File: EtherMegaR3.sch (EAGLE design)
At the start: 49 parts, among them IC2 APX811-44UG-7, IC4 MCP24AA025E48, IC6 W5100SQFP80, IC9 ATMEGA2560-16AU, Q3 2N7002, U1 HY931147C-RJ45, X2 25MHz, X3 16MHz

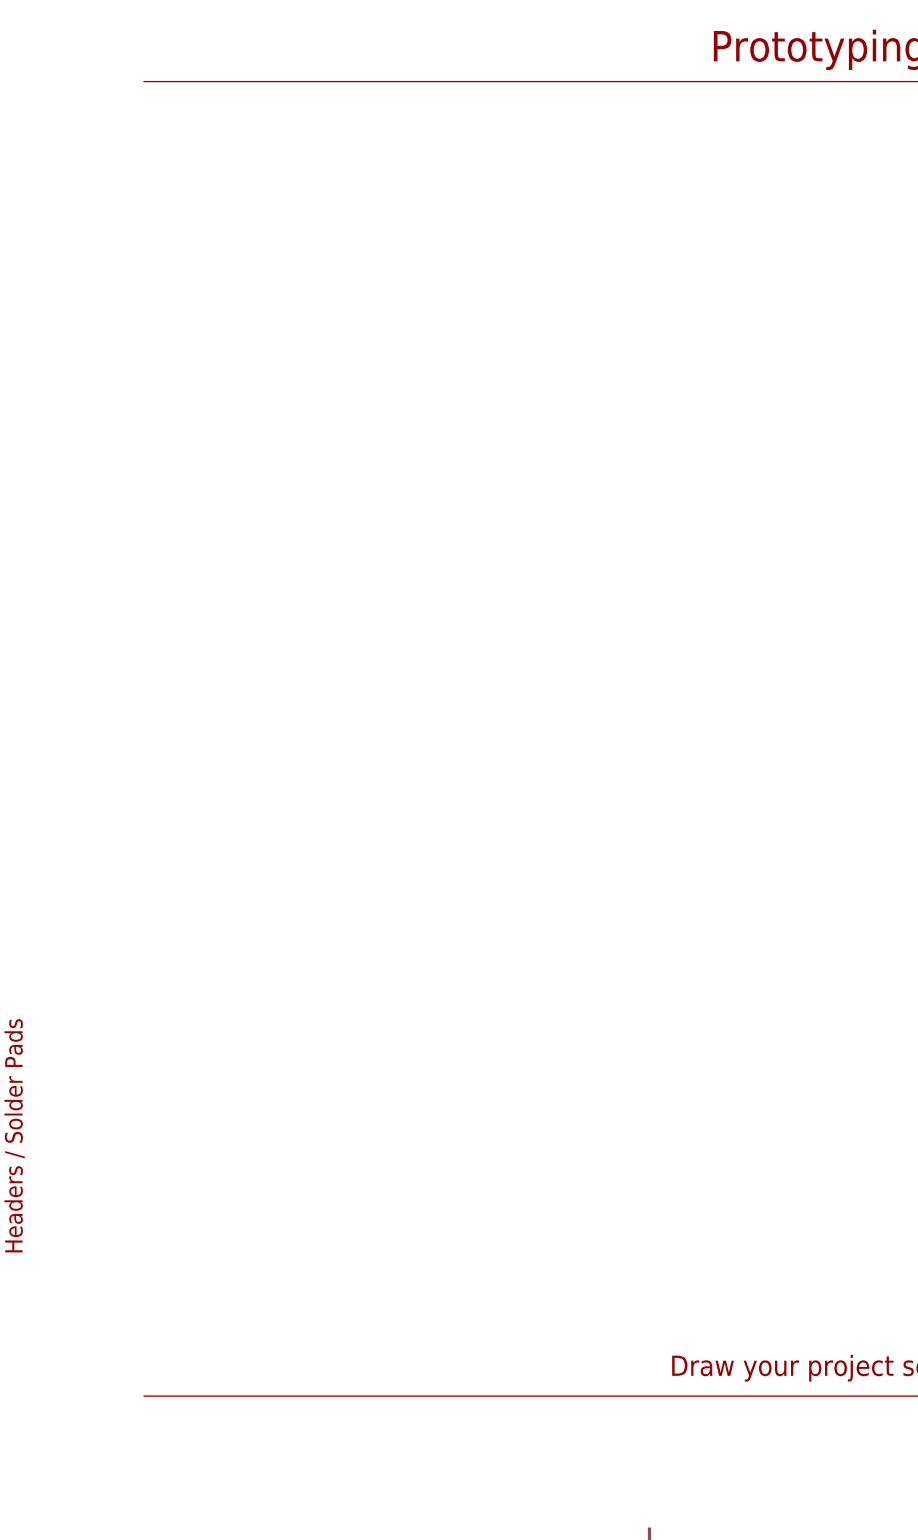
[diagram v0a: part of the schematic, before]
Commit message: remove eagle.epf
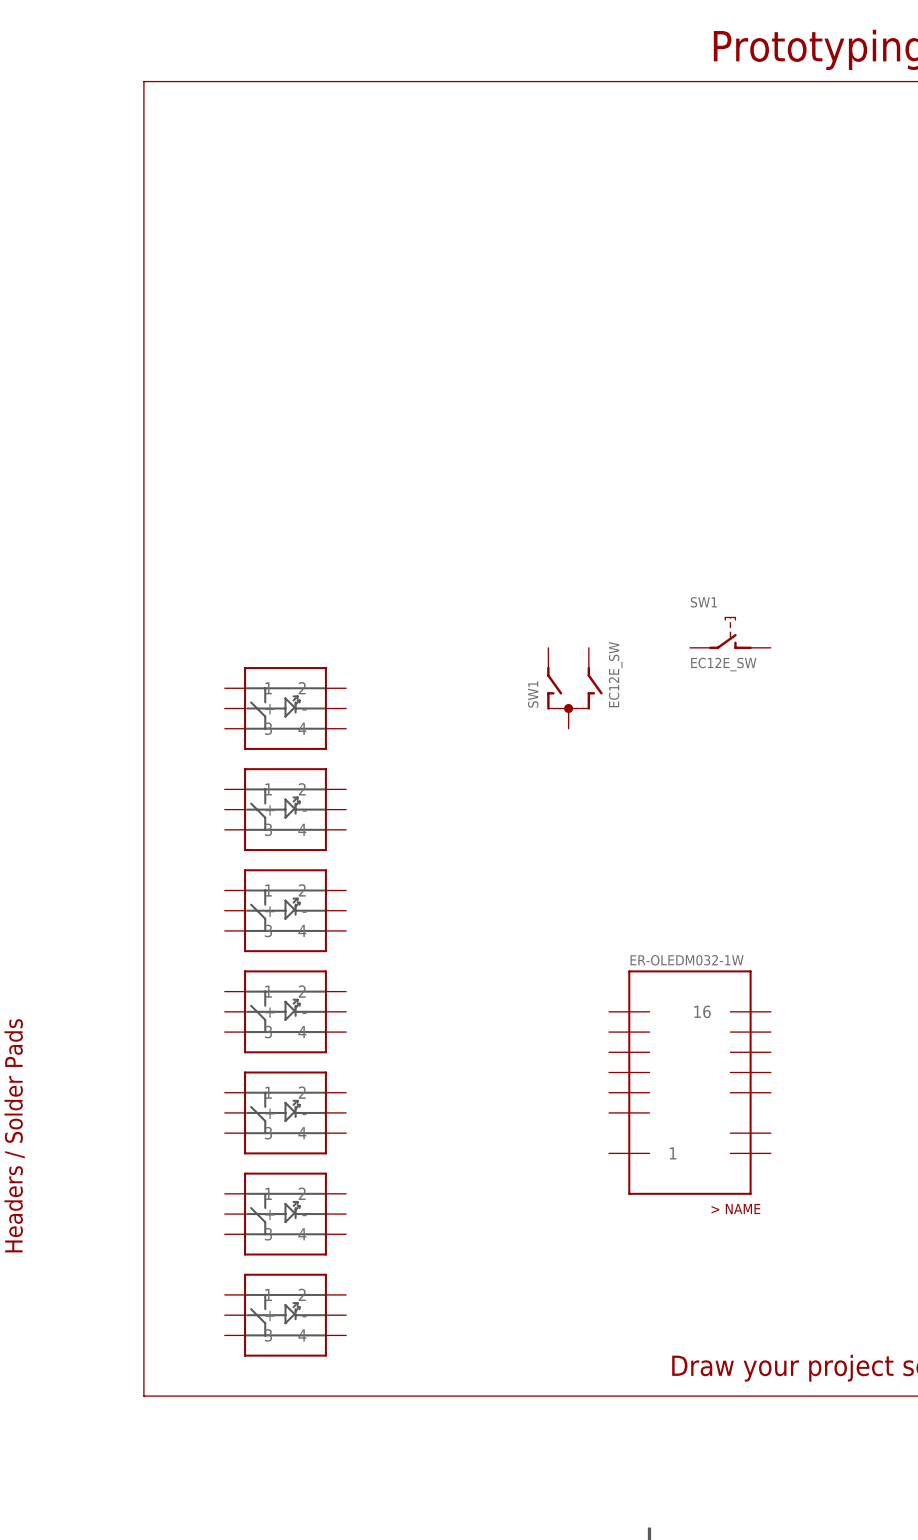
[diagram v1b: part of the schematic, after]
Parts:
- added BTN_FAVE1, BTN_FAVE2, BTN_FAVE3, BTN_FAVE4, BTN_FAVE5, BTN_MODE, BTN_OFF: PB614, RSJ-PB614:PB614
- added SW1: EC12E_SW, switch-alps:EC12E_SW
- added U$1: ER-OLED-M032-1W, Mat-Library:ER-OLED-M032-1W
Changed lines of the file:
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@@
 <layer number="54" name="bGND_GNDA" color="1" fill="9" visible="no" active="no"/>
 <layer number="56" name="wert" color="7" fill="1" visible="no" active="no"/>
+<layer number="90" name="Modules" color="5" fill="1" visible="yes" active="yes"/>
 <layer number="91" name="Nets" color="2" fill="1" visible="yes" active="yes"/>
 <layer number="92" name="Busses" color="1" fill="1" visible="yes" active="yes"/>
@@
 <part name="SJ5" library="freetronics-jon" deviceset="SJC" device="N" value=""/>
 <part name="SJ6" library="freetronics-jon" deviceset="SJC" device="N" value=""/>
+<part name="BTN_FAVE1" library="RSJ-PB614" deviceset="PB614" device=""/>
+<part name="BTN_FAVE2" library="RSJ-PB614" deviceset="PB614" device=""/>
+<part name="BTN_FAVE3" library="RSJ-PB614" deviceset="PB614" device=""/>
+<part name="BTN_FAVE4" library="RSJ-PB614" deviceset="PB614" device=""/>
+<part name="BTN_FAVE5" library="RSJ-PB614" deviceset="PB614" device=""/>
+<part name="BTN_MODE" library="RSJ-PB614" deviceset="PB614" device=""/>
+<part name="BTN_OFF" library="RSJ-PB614" deviceset="PB614" device=""/>
+<part name="U$1" library="Mat-Library" deviceset="ER-OLED-M032-1W" device=""/>
+<part name="SW1" library="switch-alps" deviceset="EC12E_SW" device=""/>
 </parts>
 <sheets>
@@
 <wire x1="416.56" y1="59.69" x2="416.56" y2="21.59" width="0.4064" layer="97" style="longdash"/>
 <wire x1="462.28" y1="69.85" x2="417.83" y2="69.85" width="0.4064" layer="97" style="longdash"/>
+<wire x1="25.4" y1="198.12" x2="25.4" y2="363.22" width="0.1524" layer="94"/>
 </plain>
 <instances>
@@
 <instance part="SJ5" gate="G$1" x="449.58" y="297.18"/>
 <instance part="SJ6" gate="G$1" x="449.58" y="289.56"/>
+<instance part="BTN_FAVE1" gate="G$1" x="40.64" y="208.28"/>
+<instance part="BTN_FAVE2" gate="G$1" x="40.64" y="220.98"/>
+<instance part="BTN_FAVE3" gate="G$1" x="40.64" y="233.68"/>
+<instance part="BTN_FAVE4" gate="G$1" x="40.64" y="246.38"/>
+<instance part="BTN_FAVE5" gate="G$1" x="40.64" y="259.08"/>
+<instance part="BTN_MODE" gate="G$1" x="40.64" y="271.78"/>
+<instance part="BTN_OFF" gate="G$1" x="40.64" y="284.48"/>
+<instance part="U$1" gate="G$1" x="93.98" y="236.22"/>
+<instance part="SW1" gate="G$1" x="78.74" y="284.48"/>
+<instance part="SW1" gate="G$2" x="99.06" y="292.1"/>
 </instances>
 <busses>

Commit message: - Finished placing physical dimensions (button holes, faceplate outlines) - Added Fleetwood components - Added signal level converter (based on Sparkfun bi-directional converter) - Removed REG1 in 3v3 power supply as we will use only the bigger SOT223 one - Placed WIZNET and ATMEGA chips and most of their associated components onto relevant side of board - Positioned Fleetwood components - Have not yet included MPR121 cap sense - Have not yet positioned WIZNET and ATMEGA chips and components in proper locations
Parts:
- removed REG1: LD1117-SOT89, freetronics:V_REG_LM1117SOT89
- removed U$1: ER-OLED-M032-1W, Mat-Library:ER-OLED-M032-1W
- added OLED: ER-OLED-M032-1W, Mat-Library:ER-OLED-M032-1W
- added OLED_CLK, OLED_CS, OLED_DATA, OLED_DS: BSS138, SparkFun:MOSFET-NCHANNELSMD
- added R20, R21, R22, R23, R24, R25, R26, R27: 10k, freetronics-marc:RESISTOR0603
- added R28, R29, R30, R31, R32, R33, R34: 100R, freetronics-marc:RESISTOR0603
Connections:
- new net ADC8: BTN_FAVE5.1
- new net ADC9: BTN_FAVE5.+
- new net N$10: BTN_FAVE4.-, R31.2
- new net N$11: BTN_FAVE5.-, R32.2
- new net N$12: BTN_MODE.-, R33.2
- new net N$13: BTN_OFF.-, R34.2
- new net N$2: BTN_FAVE1.-, R28.2
- new net N$3: OLED.4, OLED_CLK.S, R20.1
- new net N$4: OLED.5, OLED_DATA.S, R22.1
- new net N$5: BTN_FAVE2.-, R29.2
- new net N$6: OLED.14, OLED_DS.S, R24.1
- new net N$7: BTN_FAVE3.-, R30.2
- new net N$8: OLED.16, OLED_CS.S, R26.1
- net 3V3D: now also R20.2, R22.2, R24.2, R26.2; no longer REG1.OUT, REG1.OUT@1
- net 5V: now also OLED.15, OLED.2, R21.2, R23.2, R25.2, R27.2; no longer REG1.IN
- net A10: now also BTN_MODE.1
- net A11: now also BTN_MODE.+
- net A13: now also BTN_OFF.1
- net A14: now also BTN_OFF.+
- net ADC0: now also BTN_FAVE1.1
- net ADC1: now also BTN_FAVE1.+
- net ADC2: now also BTN_FAVE2.1
- net ADC3: now also BTN_FAVE2.+
- net ADC4: now also BTN_FAVE3.1
- net ADC5: now also BTN_FAVE3.+
- net ADC6: now also BTN_FAVE4.1
- net ADC7: now also BTN_FAVE4.+
- net D2: now also SW1G$1.A
- net D3: now also SW1G$1.B
- net D4: now also OLED_CLK.D, R21.1
- net D5: now also OLED_DATA.D, R23.1
- net D6: now also OLED_CS.D, R27.1
- net D7: now also OLED_DS.D, R25.1
- net D8: now also SW1G$2.1
- net GND: now also BTN_FAVE1.4, BTN_FAVE2.4, BTN_FAVE3.4, BTN_FAVE4.4, BTN_FAVE5.4, BTN_MODE.4, BTN_OFF.4, OLED.1, OLED.10, OLED.11, OLED.12, OLED.13, OLED.7, OLED.8, OLED.9, R28.1, R29.1, R30.1, R31.1, R32.1, R33.1, R34.1, SW1G$1.C, SW1G$2.2; no longer REG1.ADJ
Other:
- note added: "BTN 1"
- note added: "BTN 2"
- note added: "BTN 3"
- note added: "BTN 4"
- note added: "BTN 5"
- note added: "BTN All Off"
- note added: "BTN Mode"
- note added: "OLED"
- note added: "Rotary Encoder"
- note added: "Signal Level Converters"
- note removed: "Draw your project schematic here"
- note removed: "Dual Footprint"
- moved on the sheet: SW1

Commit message: minor eagle updates
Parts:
- removed RN2: 1K, freetronics-master-v1:4R-NCAY16
- added RN2A, RN2B: 1k, freetronics-marc:RESISTOR0603
- added U$1: EUP3476SO08T, freetronics-jon:EUP3476SO08T
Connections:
- net FDXLED: now also RN2A.1; no longer RN2A.2
- net LINKLED: now also RN2B.1; no longer RN2B.2
- net N$332: now also RN2B.2; no longer RN2B.1
- net N$67: now also RN2A.2; no longer RN2A.1
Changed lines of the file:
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@@
 <part name="GND35" library="SparkFun" deviceset="GND" device=""/>
 <part name="R7" library="freetronics-marc" deviceset="RESISTOR" device="0603" value="1M 0603"/>
-<part name="RN2" library="freetronics-master-v1" deviceset="4R-N" device="CAY16" value="1K"/>
 <part name="RN5" library="freetronics-master-v1" deviceset="4R-N" device="CAY16" value="49R9 1%"/>
 <part name="C9" library="freetronics-marc" deviceset="CAP" device="0603" value="1uF 0603"/>
@@
 <part name="R33" library="freetronics-marc" deviceset="RESISTOR" device="0603" value="100R"/>
 <part name="R34" library="freetronics-marc" deviceset="RESISTOR" device="0603" value="100R"/>
+<part name="RN2A" library="freetronics-marc" deviceset="RESISTOR" device="0603" value="1k"/>
+<part name="RN2B" library="freetronics-marc" deviceset="RESISTOR" device="0603" value="1k"/>
+<part name="U$1" library="freetronics-jon" deviceset="EUP3476" device="SO08T"/>
 </parts>
 <sheets>
@@
 <attribute name="VALUE" x="434.848" y="83.312" size="1.778" layer="96"/>
 </instance>
-<instance part="RN2" gate="A" x="93.98" y="96.52"/>
-<instance part="RN2" gate="B" x="93.98" y="88.9"/>
 <instance part="RN5" gate="A" x="104.14" y="63.5" smashed="yes" rot="R270">
 <attribute name="NAME" x="102.108" y="60.96" size="1.778" layer="95" rot="R90"/>
@@
 <attribute name="VALUE" x="62.23" y="282.702" size="1.778" layer="96" rot="R180"/>
 </instance>
+<instance part="RN2A" gate="G$1" x="93.98" y="96.52" smashed="yes" rot="R180">
+<attribute name="NAME" x="97.79" y="92.4814" size="1.778" layer="95" rot="R180"/>
+<attribute name="VALUE" x="97.79" y="94.742" size="1.778" layer="96" rot="R180"/>
+</instance>
+<instance part="RN2B" gate="G$1" x="93.98" y="88.9" smashed="yes" rot="R180">
+<attribute name="NAME" x="97.79" y="84.8614" size="1.778" layer="95" rot="R180"/>
+<attribute name="VALUE" x="97.79" y="87.122" size="1.778" layer="96" rot="R180"/>
+</instance>
+<instance part="U$1" gate="G$1" x="340.36" y="149.86"/>
 </instances>
 <busses>
@@
 <wire x1="99.06" y1="88.9" x2="113.03" y2="88.9" width="0.1524" layer="91"/>
 <label x="102.87" y="88.9" size="1.778" layer="95"/>
-<pinref part="RN2" gate="B" pin="2"/>
+<pinref part="RN2B" gate="G$1" pin="1"/>
 </segment>
 <segment>
@@
 <wire x1="99.06" y1="96.52" x2="113.03" y2="96.52" width="0.1524" layer="91"/>
 <label x="102.87" y="96.52" size="1.778" layer="95"/>
-<pinref part="RN2" gate="A" pin="2"/>
+<pinref part="RN2A" gate="G$1" pin="1"/>
 </segment>
 </net>
@@
 <wire x1="88.9" y1="88.9" x2="73.66" y2="88.9" width="0.1524" layer="91"/>
 <pinref part="U1" gate="G$1" pin="Y-"/>
-<pinref part="RN2" gate="B" pin="1"/>
+<pinref part="RN2B" gate="G$1" pin="2"/>
 </segment>
 </net>
@@
 <wire x1="73.66" y1="96.52" x2="88.9" y2="96.52" width="0.1524" layer="91"/>
 <pinref part="U1" gate="G$1" pin="G-"/>
-<pinref part="RN2" gate="A" pin="1"/>
-</segment>
-</net>
+<pinref part="RN2A" gate="G$1" pin="2"/>
+</segment>
+</net>
